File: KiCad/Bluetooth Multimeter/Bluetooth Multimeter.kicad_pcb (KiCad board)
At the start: 2 copper layers, 55 x 90 mm, 30 parts, among them J1 V/Ohm, J2 Com, J3 mA, J4 A, J5 Parallel Prot, K1 Low Range, K2 Medium Range, K3 High Range, K4 UH Range (Ohm Only), K5 V/Ohm Switch, U1 ItsyBitsy_NRF52840_Big

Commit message: Slightly Modifided PCB
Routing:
- net /V/Ohm In: track 60.1 -> 73.1 mm, vias 2 -> 1
- net /A ADC In: track 91.8 -> 87.1 mm
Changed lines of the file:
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@@
   (segment (start 216.408 138.176) (end 219.456 135.128) (width 1) (layer "B.Cu") (net 14))
   (segment (start 223.002 102.88) (end 217.474012 102.88) (width 5) (layer "F.Cu") (net 15))
+  (segment (start 220.756 121.92) (end 214.376 121.92) (width 5) (layer "F.Cu") (net 15))
+  (segment (start 214.376 121.92) (end 210.312 125.984) (width 5) (layer "F.Cu") (net 15))
   (segment (start 213.614 92.456) (end 213.614 101.244) (width 0.4) (layer "F.Cu") (net 15))
+  (segment (start 226.314 116.362) (end 220.756 121.92) (width 5) (layer "F.Cu") (net 15))
   (segment (start 200.66 86.868) (end 208.026 86.868) (width 0.4) (layer "F.Cu") (net 15))
   (segment (start 213.614 101.244) (end 216.002 103.632) (width 0.4) (layer "F.Cu") (net 15))
@@
   (segment (start 226.314 117.08191) (end 226.673955 116.721955) (width 5) (layer "B.Cu") (net 15))
   (segment (start 224.012 125.984) (end 224.012 122.698) (width 5) (layer "B.Cu") (net 15))
-  (segment (start 212.852 112.014) (end 212.852 106.782) (width 0.4) (layer "B.Cu") (net 15))
   (segment (start 219.304 103.632) (end 216.002 103.632) (width 0.4) (layer "B.Cu") (net 15))
-  (segment (start 210.312 125.984) (end 210.312 114.554) (width 0.4) (layer "B.Cu") (net 15))
   (segment (start 198.12 84.328) (end 198.12 82.296) (width 0.4) (layer "B.Cu") (net 15))
   (segment (start 200.64125 86.84925) (end 200.66 86.868) (width 0.4) (layer "B.Cu") (net 15))
   (segment (start 224.012 122.698) (end 226.314 120.396) (width 5) (layer "B.Cu") (net 15))
-  (segment (start 212.852 106.782) (end 216.002 103.632) (width 0.4) (layer "B.Cu") (net 15))
-  (segment (start 210.312 114.554) (end 212.852 112.014) (width 0.4) (layer "B.Cu") (net 15))
   (segment (start 187.452 56.134) (end 187.452 56.388) (width 0.4) (layer "B.Cu") (net 16))
   (segment (start 187.452 56.388) (end 198.12 67.056) (width 0.4) (layer "B.Cu") (net 16))
@@
   (segment (start 180.376467 125.984) (end 178.952 124.559533) (width 5) (layer "B.Cu") (net 24))
   (segment (start 178.952 124.559533) (end 178.952 123.698) (width 5) (layer "B.Cu") (net 24))
-  (segment (start 209.042 120.142) (end 230.378 120.142) (width 0.4) (layer "F.Cu") (net 25))
-  (segment (start 205.994 117.094) (end 209.042 120.142) (width 0.4) (layer "F.Cu") (net 25))
-  (via (at 205.994 117.094) (size 1) (drill 0.75) (layers "F.Cu" "B.Cu") (net 25))
-  (via (at 230.378 120.142) (size 1) (drill 0.75) (layers "F.Cu" "B.Cu") (net 25))
+  (segment (start 208.28 132.08) (end 205.74 129.54) (width 0.4) (layer "F.Cu") (net 25))
+  (segment (start 223.246 132.08) (end 208.28 132.08) (width 0.4) (layer "F.Cu") (net 25))
+  (segment (start 230.378 124.948) (end 223.246 132.08) (width 0.4) (layer "F.Cu") (net 25))
+  (segment (start 205.74 129.54) (end 205.74 116.84) (width 0.4) (layer "F.Cu") (net 25))
+  (segment (start 230.378 123.698) (end 230.378 124.948) (width 0.4) (layer "F.Cu") (net 25))
+  (via (at 205.74 116.84) (size 1) (drill 0.75) (layers "F.Cu" "B.Cu") (net 25))
   (segment (start 179.832 113.441) (end 181.61 115.219) (width 0.4) (layer "B.Cu") (net 25))
-  (segment (start 183.485 117.094) (end 205.994 117.094) (width 0.4) (layer "B.Cu") (net 25))
+  (segment (start 205.74 116.84) (end 183.231 116.84) (width 0.4) (layer "B.Cu") (net 25))
   (segment (start 179.832 110.236) (end 179.832 113.441) (width 0.4) (layer "B.Cu") (net 25))
-  (segment (start 230.378 120.142) (end 230.378 123.698) (width 0.4) (layer "B.Cu") (net 25))
-  (segment (start 181.61 115.219) (end 183.485 117.094) (width 0.4) (layer "B.Cu") (net 25))
+  (segment (start 183.231 116.84) (end 181.61 115.219) (width 0.4) (layer "B.Cu") (net 25))
   (segment (start 188.2305 91.2075) (end 187.955 90.932) (width 0.4) (layer "F.Cu") (net 26))
   (segment (start 195.58 91.186) (end 195.5585 91.2075) (width 0.4) (layer "F.Cu") (net 26))
@@
   (segment (start 187.955 91.44) (end 187.955 90.932) (width 0.4) (layer "B.Cu") (net 26))
   (segment (start 200.914 91.44) (end 204.47 94.996) (width 0.4) (layer "B.Cu") (net 26))
-  (segment (start 178.432 103.756) (end 178.432 86.011767) (width 0.4) (layer "B.Cu") (net 27))
-  (segment (start 178.432 86.011767) (end 181.63 82.813767) (width 0.4) (layer "B.Cu") (net 27))
+  (segment (start 181.63 85.211884) (end 181.63 70.846) (width 0.4) (layer "B.Cu") (net 27))
   (segment (start 181.63 70.846) (end 185.42 67.056) (width 0.4) (layer "B.Cu") (net 27))
+  (segment (start 178.432 88.409884) (end 181.63 85.211884) (width 0.4) (layer "B.Cu") (net 27))
   (segment (start 184.404 109.728) (end 179.832 105.156) (width 0.4) (layer "B.Cu") (net 27))
+  (segment (start 178.432 103.756) (end 178.432 88.409884) (width 0.4) (layer "B.Cu") (net 27))
   (segment (start 184.404 111.76) (end 184.404 109.728) (width 0.4) (layer "B.Cu") (net 27))
   (segment (start 179.832 105.156) (end 178.432 103.756) (width 0.4) (layer "B.Cu") (net 27))
-  (segment (start 181.63 82.813767) (end 181.63 70.846) (width 0.4) (layer "B.Cu") (net 27))
   (segment (start 191.75 102.382) (end 191.75 70.846) (width 0.4) (layer "B.Cu") (net 28))
   (segment (start 191.75 70.846) (end 187.96 67.056) (width 0.4) (layer "B.Cu") (net 28))
@@
   (segment (start 185.674 101.854) (end 188.976 105.156) (width 0.4) (layer "B.Cu") (net 28))
   (segment (start 188.976 105.156) (end 191.75 102.382) (width 0.4) (layer "B.Cu") (net 28))
-  (segment (start 193.926 103.756) (end 193.926 83.177767) (width 0.4) (layer "B.Cu") (net 29))
+  (segment (start 194.31 85.976) (end 194.31 70.866) (width 0.4) (layer "B.Cu") (net 29))
+  (segment (start 193.926 86.36) (end 194.31 85.976) (width 0.4) (layer "B.Cu") (net 29))
+  (segment (start 199.898 111.76) (end 199.898 109.728) (width 0.4) (layer "B.Cu") (net 29))
+  (segment (start 193.926 103.756) (end 193.926 86.36) (width 0.4) (layer "B.Cu") (net 29))
+  (segment (start 199.898 109.728) (end 195.326 105.156) (width 0.4) (layer "B.Cu") (net 29))
   (segment (start 194.31 70.866) (end 190.5 67.056) (width 0.4) (layer "B.Cu") (net 29))
-  (segment (start 199.898 111.76) (end 199.898 109.728) (width 0.4) (layer "B.Cu") (net 29))
-  (segment (start 199.898 109.728) (end 195.326 105.156) (width 0.4) (layer "B.Cu") (net 29))
-  (segment (start 194.31 82.793767) (end 194.31 70.866) (width 0.4) (layer "B.Cu") (net 29))
   (segment (start 195.326 105.156) (end 193.926 103.756) (width 0.4) (layer "B.Cu") (net 29))
-  (segment (start 193.926 83.177767) (end 194.31 82.793767) (width 0.4) (layer "B.Cu") (net 29))
   (segment (start 199.898 101.854) (end 201.168 101.854) (width 0.4) (layer "B.Cu") (net 30))
   (segment (start 205.87 103.756) (end 205.87 93.602) (width 0.4) (layer "B.Cu") (net 30))

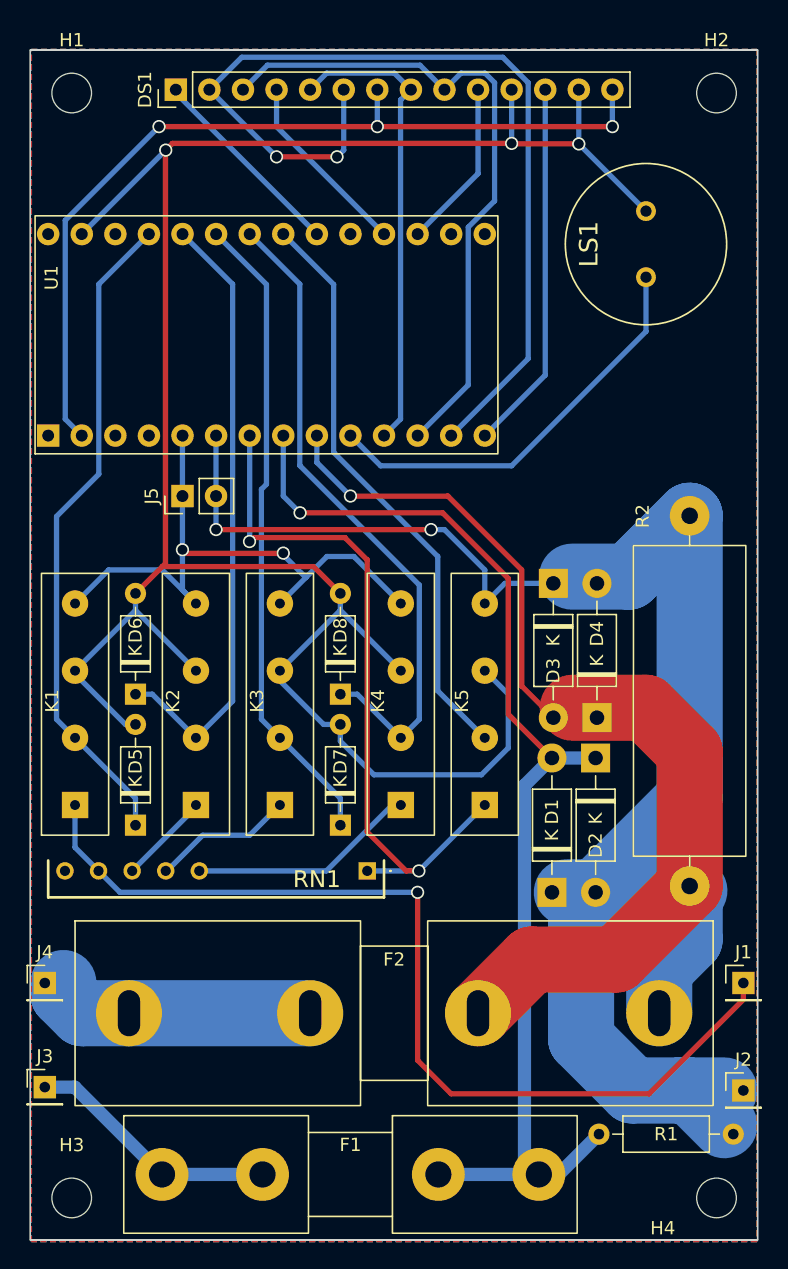
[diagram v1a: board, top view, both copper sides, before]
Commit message: began main arduino project, modified KiCad itsybitsy symbol
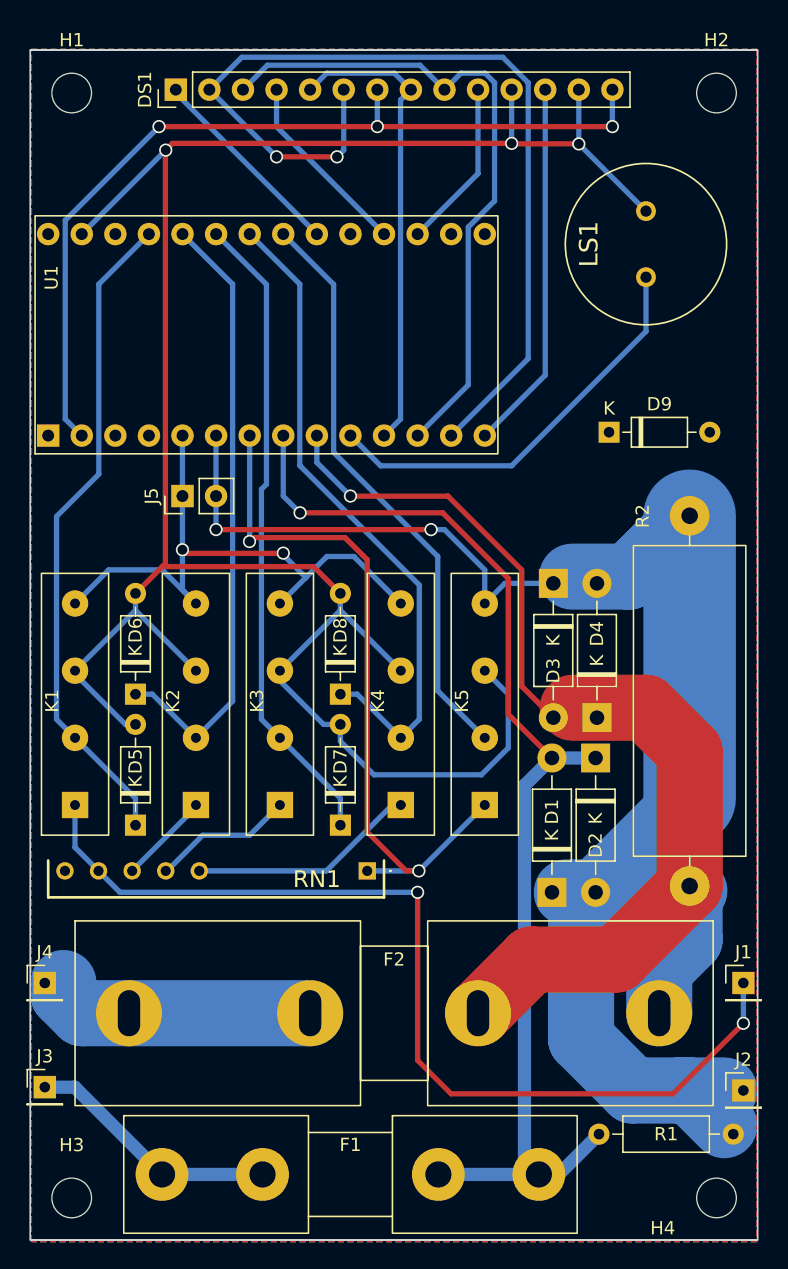
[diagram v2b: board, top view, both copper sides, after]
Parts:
- added D9: 1N4148, Diode_THT:D_DO-35_SOD27_P7.62mm_Horizontal, F.Cu at (220.2, 82.0)
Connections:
- net Net-(U1-A5) renamed /Speaker Control
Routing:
- net /V/Ohm In: track 73.1 -> 74.2 mm, vias 1 -> 2
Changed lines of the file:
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@@
   (net 5 "unconnected-(U1-Enable-Pad3)")
   (net 6 "unconnected-(U1-VHI-Pad4)")
-  (net 7 "Net-(U1-A5)")
+  (net 7 "/Speaker Control")
   (net 8 "unconnected-(U1-RX{slash}0-Pad15)")
   (net 9 "unconnected-(U1-TX{slash}1-Pad16)")
@@
     )
   )
+  (footprint "Diode_THT:D_DO-35_SOD27_P7.62mm_Horizontal" (layer "F.Cu")
+    (at 220.218 82.042)
+    (descr "Diode, DO-35_SOD27 series, Axial, Horizontal, pin pitch=7.62mm, , length*diameter=4*2mm^2, , http://www.diodes.com/_files/packages/DO-35.pdf")
+    (tags "Diode DO-35_SOD27 series Axial Horizontal pin pitch 7.62mm  length 4mm diameter 2mm")
+    (property "Sheetfile" "Bluetooth Multimeter.kicad_sch")
+    (property "Sheetname" "")
+    (property "Sim.Device" "D")
+    (property "Sim.Pins" "1=K 2=A")
+    (property "ki_description" "100V 0.15A standard switching diode, DO-35")
+    (property "ki_keywords" "diode")
+    (attr through_hole)
+    (fp_text reference "D9" (at 3.81 -2.12) (layer "F.SilkS")
+        (effects (font (size 1 1) (thickness 0.15)))
+    )
+    (fp_text value "1N4148" (at 3.81 2.12) (layer "F.Fab")
+        (effects (font (size 1 1) (thickness 0.15)))
+    )
+    (fp_text user "K" (at 0 -1.8) (layer "F.SilkS")
+        (effects (font (size 1 1) (thickness 0.15)))
+    )
+    (fp_text user "K" (at 0 -1.8) (layer "F.Fab")
+        (effects (font (size 1 1) (thickness 0.15)))
+    )
+    (fp_text user "${REFERENCE}" (at 4.11 0) (layer "F.Fab")
+        (effects (font (size 0.8 0.8) (thickness 0.12)))
+    )
+    (fp_line (start 1.04 0) (end 1.69 0)
+      (stroke (width 0.12) (type solid)) (layer "F.SilkS"))
+    (fp_line (start 1.69 -1.12) (end 1.69 1.12)
+      (stroke (width 0.12) (type solid)) (layer "F.SilkS"))
+    (fp_line (start 1.69 1.12) (end 5.93 1.12)
+      (stroke (width 0.12) (type solid)) (layer "F.SilkS"))
+    (fp_line (start 2.29 -1.12) (end 2.29 1.12)
+      (stroke (width 0.12) (type solid)) (layer "F.SilkS"))
+    (fp_line (start 2.41 -1.12) (end 2.41 1.12)
+      (stroke (width 0.12) (type solid)) (layer "F.SilkS"))
+    (fp_line (start 2.53 -1.12) (end 2.53 1.12)
+      (stroke (width 0.12) (type solid)) (layer "F.SilkS"))
+    (fp_line (start 5.93 -1.12) (end 1.69 -1.12)
+      (stroke (width 0.12) (type solid)) (layer "F.SilkS"))
+    (fp_line (start 5.93 1.12) (end 5.93 -1.12)
+      (stroke (width 0.12) (type solid)) (layer "F.SilkS"))
+    (fp_line (start 6.58 0) (end 5.93 0)
+      (stroke (width 0.12) (type solid)) (layer "F.SilkS"))
+    (fp_line (start -1.05 -1.25) (end -1.05 1.25)
+      (stroke (width 0.05) (type solid)) (layer "F.CrtYd"))
+    (fp_line (start -1.05 1.25) (end 8.67 1.25)
+      (stroke (width 0.05) (type solid)) (layer "F.CrtYd"))
+    (fp_line (start 8.67 -1.25) (end -1.05 -1.25)
+      (stroke (width 0.05) (type solid)) (layer "F.CrtYd"))
+    (fp_line (start 8.67 1.25) (end 8.67 -1.25)
+      (stroke (width 0.05) (type solid)) (layer "F.CrtYd"))
+    (fp_line (start 0 0) (end 1.81 0)
+      (stroke (width 0.1) (type solid)) (layer "F.Fab"))
+    (fp_line (start 1.81 -1) (end 1.81 1)
+      (stroke (width 0.1) (type solid)) (layer "F.Fab"))
+    (fp_line (start 1.81 1) (end 5.81 1)
+      (stroke (width 0.1) (type solid)) (layer "F.Fab"))
+    (fp_line (start 2.31 -1) (end 2.31 1)
+      (stroke (width 0.1) (type solid)) (layer "F.Fab"))
+    (fp_line (start 2.41 -1) (end 2.41 1)
+      (stroke (width 0.1) (type solid)) (layer "F.Fab"))
+    (fp_line (start 2.51 -1) (end 2.51 1)
+      (stroke (width 0.1) (type solid)) (layer "F.Fab"))
+    (fp_line (start 5.81 -1) (end 1.81 -1)
+      (stroke (width 0.1) (type solid)) (layer "F.Fab"))
+    (fp_line (start 5.81 1) (end 5.81 -1)
+      (stroke (width 0.1) (type solid)) (layer "F.Fab"))
+    (fp_line (start 7.62 0) (end 5.81 0)
+      (stroke (width 0.1) (type solid)) (layer "F.Fab"))
+    (pad "1" thru_hole rect (at 0 0) (size 1.6 1.6) (drill 0.8) (layers "*.Cu" "*.Mask")
+      (net 32 "/V{slash}Ohm Control") (pinfunction "K") (pintype "passive"))
+    (pad "2" thru_hole oval (at 7.62 0) (size 1.6 1.6) (drill 0.8) (layers "*.Cu" "*.Mask")
+      (net 2 "GND") (pinfunction "A") (pintype "passive"))
+    (model "${KICAD6_3DMODEL_DIR}/Diode_THT.3dshapes/D_DO-35_SOD27_P7.62mm_Horizontal.wrl"
+      (offset (xyz 0 0 0))
+      (scale (xyz 1 1 1))
+      (rotate (xyz 0 0 0))
+    )
+  )
   (footprint "502ProjectFootprints:SIL03-1A72-71_4" (layer "F.Cu")
     (at 210.82 102.616 90)
@@
       (stroke (width 0.127) (type solid)) (fill none) (layer "F.Fab"))
     (pad "1" thru_hole circle (at -2.5 0 90) (size 1.5 1.5) (drill 0.85) (layers "*.Cu" "*.Mask")
-      (net 7 "Net-(U1-A5)") (pintype "passive"))
+      (net 7 "/Speaker Control") (pintype "passive"))
     (pad "2" thru_hole circle (at 2.5 0 90) (size 1.5 1.5) (drill 0.85) (layers "*.Cu" "*.Mask")
       (net 2 "GND") (pintype "passive"))
@@
       (net 15 "/A ADC In") (pinfunction "A4") (pintype "input"))
     (pad "10" thru_hole circle (at -7.62 6.35 90) (size 1.7 1.7) (drill 0.9) (layers "*.Cu" "*.Mask")
-      (net 7 "Net-(U1-A5)") (pinfunction "A5") (pintype "input"))
+      (net 7 "/Speaker Control") (pinfunction "A5") (pintype "input"))
     (pad "11" thru_hole circle (at -7.62 8.89 90) (size 1.7 1.7) (drill 0.9) (layers "*.Cu" "*.Mask")
       (net 20 "/SCK") (pinfunction "SCK/25") (pintype "bidirectional"))
@@
   (segment (start 207.770957 89.406957) (end 210.82 92.456) (width 0.4) (layer "B.Cu") (net 13))
   (segment (start 212.344 93.472) (end 210.82 94.996) (width 0.4) (layer "B.Cu") (net 13))
-  (segment (start 226.314 88.362) (end 226.314 109.728) (width 5) (layer "B.Cu") (net 13))
+  (segment (start 226.314 88.362) (end 226.314 109.728) (width 7) (layer "B.Cu") (net 13))
   (segment (start 190.495 86.868) (end 190.495 82.301) (width 0.4) (layer "B.Cu") (net 13))
   (segment (start 190.495 82.301) (end 190.5 82.296) (width 0.4) (layer "B.Cu") (net 13))
@@
   (segment (start 180.376467 125.984) (end 178.952 124.559533) (width 5) (layer "B.Cu") (net 24))
   (segment (start 178.952 124.559533) (end 178.952 123.698) (width 5) (layer "B.Cu") (net 24))
+  (segment (start 225.044 132.08) (end 208.28 132.08) (width 0.4) (layer "F.Cu") (net 25))
+  (segment (start 205.74 129.54) (end 205.74 116.84) (width 0.4) (layer "F.Cu") (net 25))
+  (segment (start 230.378 126.746) (end 225.044 132.08) (width 0.4) (layer "F.Cu") (net 25))
   (segment (start 208.28 132.08) (end 205.74 129.54) (width 0.4) (layer "F.Cu") (net 25))
-  (segment (start 223.246 132.08) (end 208.28 132.08) (width 0.4) (layer "F.Cu") (net 25))
-  (segment (start 230.378 124.948) (end 223.246 132.08) (width 0.4) (layer "F.Cu") (net 25))
-  (segment (start 205.74 129.54) (end 205.74 116.84) (width 0.4) (layer "F.Cu") (net 25))
-  (segment (start 230.378 123.698) (end 230.378 124.948) (width 0.4) (layer "F.Cu") (net 25))
   (via (at 205.74 116.84) (size 1) (drill 0.75) (layers "F.Cu" "B.Cu") (net 25))
+  (via (at 230.378 126.746) (size 1) (drill 0.75) (layers "F.Cu" "B.Cu") (net 25))
   (segment (start 179.832 113.441) (end 181.61 115.219) (width 0.4) (layer "B.Cu") (net 25))
-  (segment (start 205.74 116.84) (end 183.231 116.84) (width 0.4) (layer "B.Cu") (net 25))
+  (segment (start 183.231 116.84) (end 205.74 116.84) (width 0.4) (layer "B.Cu") (net 25))
   (segment (start 179.832 110.236) (end 179.832 113.441) (width 0.4) (layer "B.Cu") (net 25))
-  (segment (start 183.231 116.84) (end 181.61 115.219) (width 0.4) (layer "B.Cu") (net 25))
+  (segment (start 181.61 115.219) (end 183.231 116.84) (width 0.4) (layer "B.Cu") (net 25))
+  (segment (start 230.378 126.746) (end 230.378 123.698) (width 0.4) (layer "B.Cu") (net 25))
   (segment (start 188.2305 91.2075) (end 187.955 90.932) (width 0.4) (layer "F.Cu") (net 26))
   (segment (start 195.58 91.186) (end 195.5585 91.2075) (width 0.4) (layer "F.Cu") (net 26))
